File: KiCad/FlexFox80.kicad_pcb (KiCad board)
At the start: 4 copper layers, 111.2 x 80 mm, 147 parts, among them J101 DIN-5_180degree, J102 Conn_01x02, J203 V4, J301 DB9_Female, J304 Conn_01x10, J305 Conn_01x02, J306 Conn_01x02, J307 Conn_01x02, J308 Conn_01x02, P203 Power Pole, P301 ISP/PDI, P302 Thru, P304 Header, Q102 IRF610, Q201 MUN5213DW1, Q202 DMP4025LSD, Q203 RJK0354DSP, Q301 PN2222A, SW301 SPST, U101 TPS22810DBVT, U107 LM5134B, U202 OPA171, U203 LTC3600, U204 MIC2196, U301 DS3231, U302 AVR128DA48, U303 LD2985BM33R, U304 SI5351A, U305 74HC1G08, U306 LT1763CS8-5, U307 TPS22810DBVT, U308 LD2985BM33R, X301 25.MHZ TCXO

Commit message: Updated Gerbers
Corrected version date on PCB
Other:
- board text added: "FlexFox80 Version 2.0 - Mar 2022"
- board text removed: "FlexFox80 Version 2.0 - Jan 2022"

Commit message: Gerber Update
o Corrected dimensions of U203
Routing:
- net +2to+12V: track 104.2 -> 106.7 mm
- net Net-(R207-Pad1): track 33.2 -> 34.0 mm

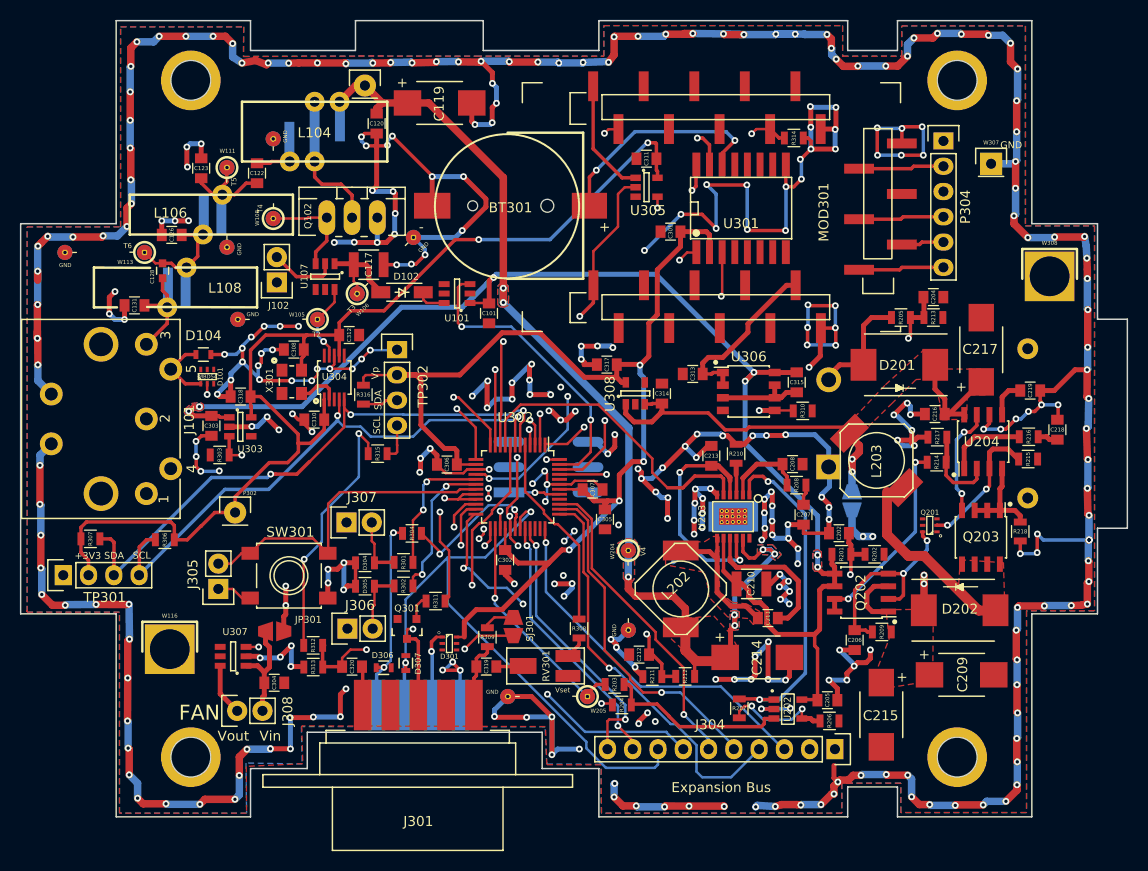
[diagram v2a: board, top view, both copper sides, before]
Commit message: Footprint Updates
Tweaks to PCB footprints.
Removed solder paste from unpopulated components
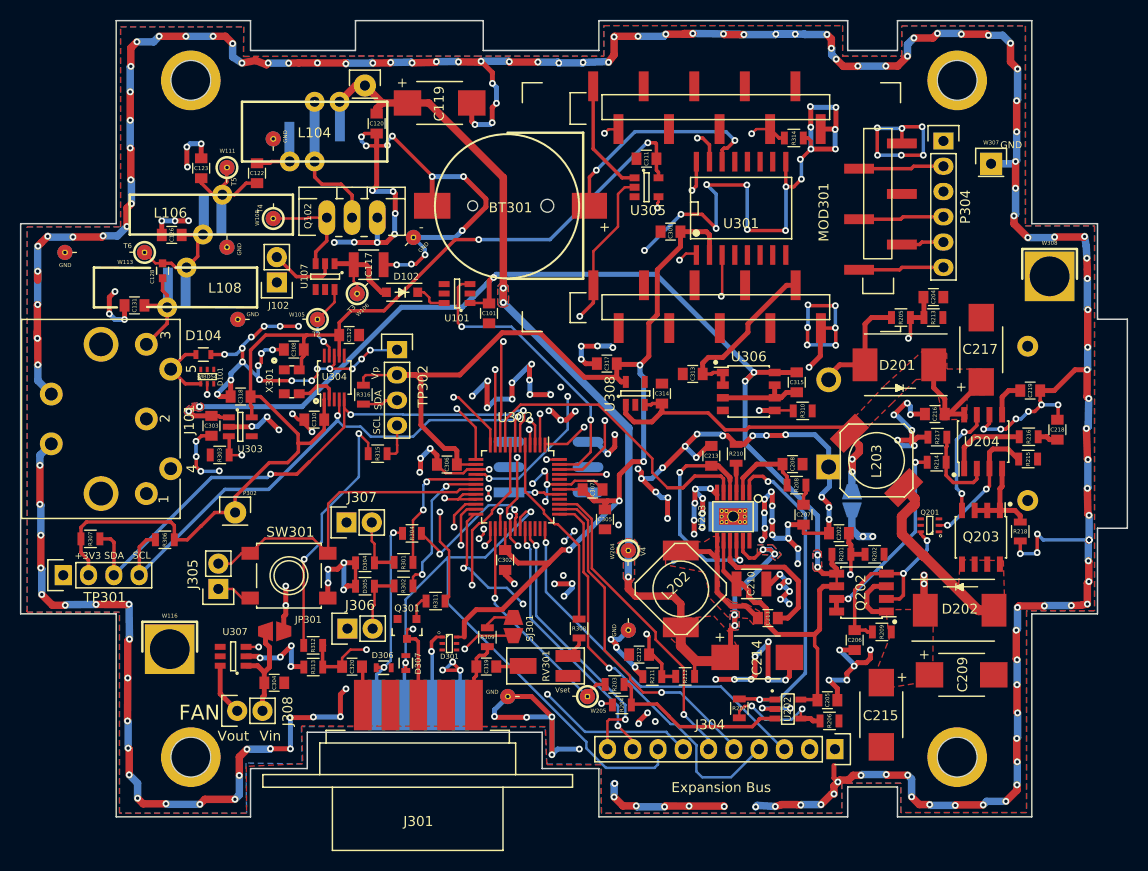
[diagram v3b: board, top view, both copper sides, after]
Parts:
- D102: footprint Diodes_SMD:SOD-123_Handsolder -> Diodes_SMD:SOD-123
- U203: footprint Housings_SSOP:SSOP-12_Pad -> Housings_SSOP:SSOP-12_Pad_Handsolder
- moved C317 0.10 mm to (75.1, 64.5)
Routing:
- net Vproc: track 183.3 -> 184.2 mm
- net RTC_SCL: track 51.8 -> 52.4 mm
- net +12V: track 174.7 -> 175.2 mm
- net Net-(C117-Pad1): track 9.65 -> 10.2 mm

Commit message: PCB Updates
Adjusted clearances on PCB. All Gerbers have been updated.
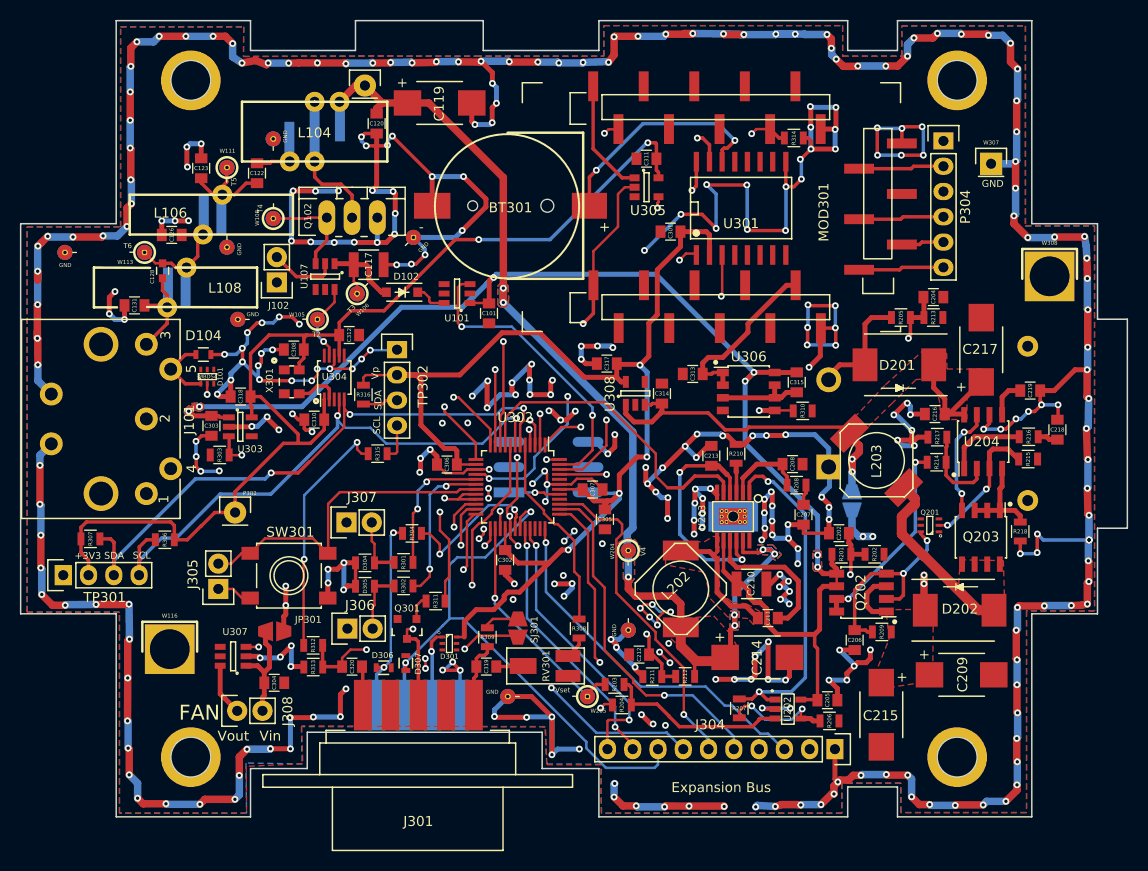
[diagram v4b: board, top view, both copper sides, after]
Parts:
- moved SJ301 0.47 mm to (66.2, 91.0)
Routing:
- net GND: track 946.1 -> 988.5 mm, vias 356 -> 373
- net RXD_TO_FTDI: track 65.5 -> 59.6 mm
- net /Digital/PF5: track 31.9 -> 33.8 mm
- net /Digital/SCL1: track 56.0 -> 57.4 mm
- net /Digital/SDA1: track 59.1 -> 60.3 mm
- net Vproc: track 184.2 -> 183.3 mm
- net RTC_SCL: track 52.4 -> 53.1 mm
- net +2to+12V: track 106.8 -> 106.1 mm
- net /Digital/PF4: track 34.6 -> 35.3 mm
- net Net-(BT301-Pad1): track 22.6 -> 23.3 mm
- net TX_FINAL_VOLTAGE_ENABLE: track 31.2 -> 31.9 mm
- net /Digital/PE3: track 27.8 -> 28.4 mm
- net PROC_PTT_OUT: track 26.5 -> 25.9 mm
- net Net-(J301-Pad3): track 20.6 -> 21.2 mm
- net /Digital/PC6: track 14.9 -> 15.4 mm
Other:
- rule pad_to_mask_clearance: 0.07 -> 0

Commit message: PCB Update
Corrected some pad spacing issues.
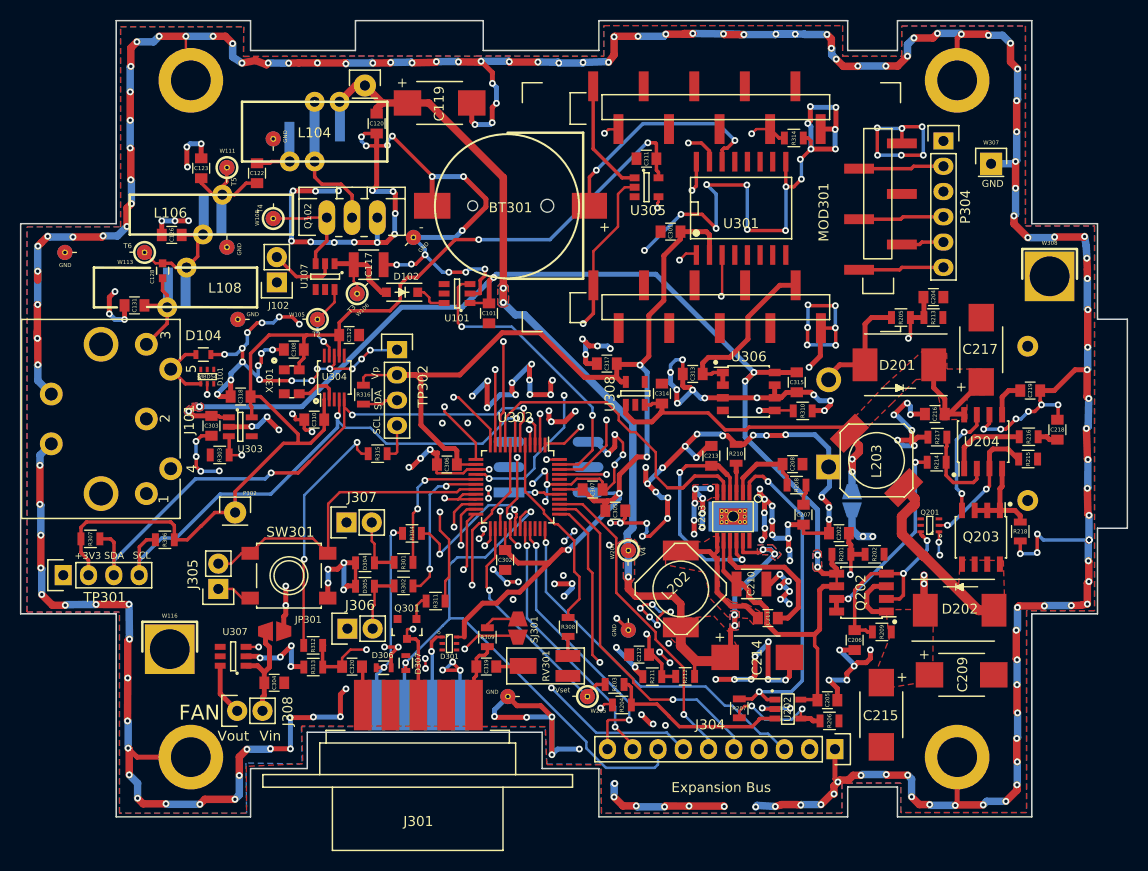
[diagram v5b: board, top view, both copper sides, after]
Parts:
- removed 4mm thru: MountingHole_4mm, Mounting_Holes:MountingHole_4mm (x4)
- added REF**: SolderWirePad_single_1mmDrill, Wire_Pads:SolderWirePad_single_1mmDrill, F.Cu at (110.3, 104.0)
- added REF**: SolderWirePad_single_1mmDrill, Wire_Pads:SolderWirePad_single_1mmDrill, F.Cu at (33.3, 104.0)
- added REF**: SolderWirePad_single_1mmDrill, Wire_Pads:SolderWirePad_single_1mmDrill, F.Cu at (33.3, 36.0)
- added REF**: SolderWirePad_single_1mmDrill, Wire_Pads:SolderWirePad_single_1mmDrill, F.Cu at (110.3, 36.0)
- moved C305 1.36 mm to (76.0, 79.2), turned to 180 degrees
- moved R308 1.11 mm to (71.2, 90.9)
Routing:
- net GND: track 988.5 -> 1068.3 mm, vias 373 -> 398
- net /Digital/PF5: track 33.8 -> 32.2 mm
- net +3V3_L8: track 191.0 -> 191.9 mm
- net Net-(C313-Pad2): track 17.6 -> 18.4 mm
- net DAC_OUTPUT: track 23.2 -> 23.9 mm
- net +2to+12V: track 106.1 -> 106.6 mm
- net RTC_SDA: track 55.6 -> 55.1 mm
- net Net-(R207-Pad1): track 34.6 -> 34.1 mm
- net /Digital/ADC7: track 54.3 -> 54.8 mm

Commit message: Updated Silkscreen
o Incremented PCB version number
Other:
- board text added: "FlexFox80 Version 2.1 - Mar 2022"
- board text removed: "FlexFox80 Version 2.0 - Mar 2022"

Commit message: Latest Gerbers
Gerbers with minor updates to silkscreen and D101, D301 footprints
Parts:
- D101, D301: footprint TO_SOT_Packages_SMD:SOT-363-0.65 -> TO_SOT_Packages_SMD:SOT-363-0.65_MBD54
- D304, D305: footprint Resistors_SMD:R_0805 -> Diodes_SMD:D_0805
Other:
- board text added: "FlexFox80 Version 2.2 - Mar 2022"
- board text removed: "FlexFox80 Version 2.1 - Mar 2022"

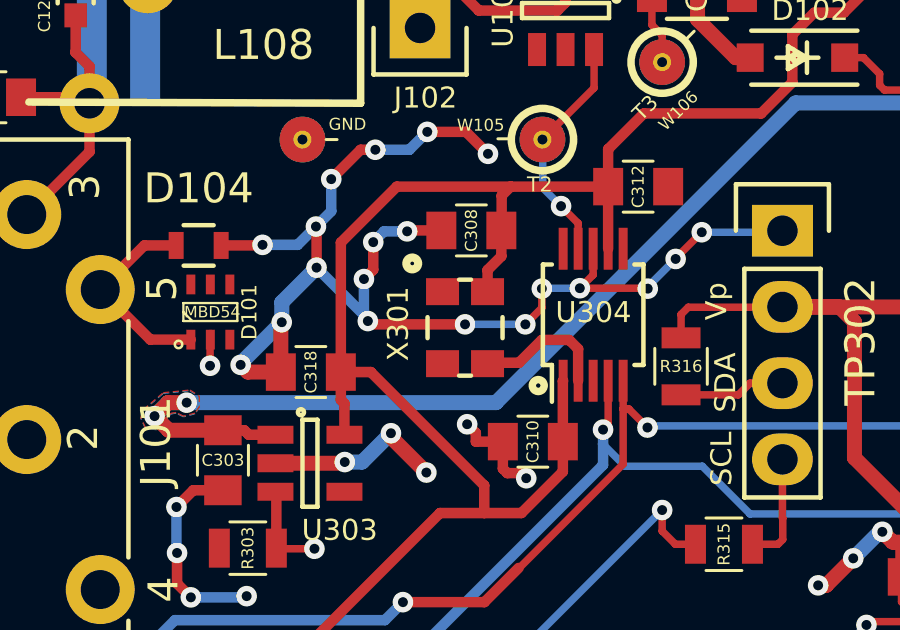
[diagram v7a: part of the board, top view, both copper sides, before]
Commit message: KiCad V6 Updates
Mostly schematic updates for KiCad V6
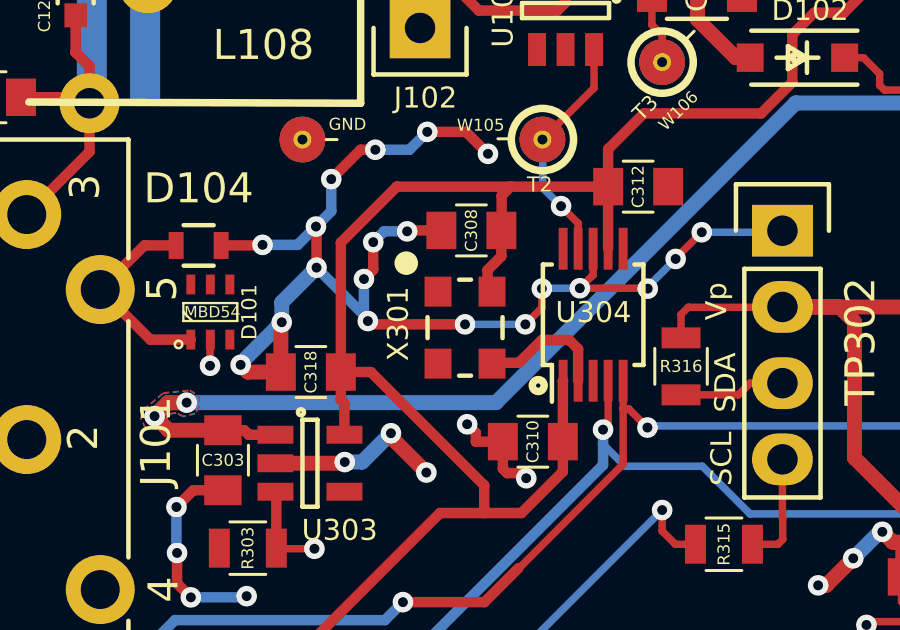
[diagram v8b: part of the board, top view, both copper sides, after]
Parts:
- X301: footprint Crystals:ASTX-H11-25.000MHZ -> Crystals:TXETCLSANF-25.000MHZ
